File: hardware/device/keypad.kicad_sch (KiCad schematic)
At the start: 42 parts, among them SW1 TRIG1, SW10 TRIG10, SW11 TRIG11, SW12 TRIG12, SW13 TRIG13, SW14 TRIG14, SW15 TRIG15, SW16 TRIG16, SW17 WHEEL_BTN, SW18 HELP, SW19 LEFT_BTN, SW2 TRIG2, SW20 RIGHT_BTN, SW3 TRIG3, SW4 TRIG4, SW5 TRIG5, SW6 TRIG6, SW7 TRIG7, SW8 TRIG8, SW9 TRIG9, U25 TCA8418RTWR

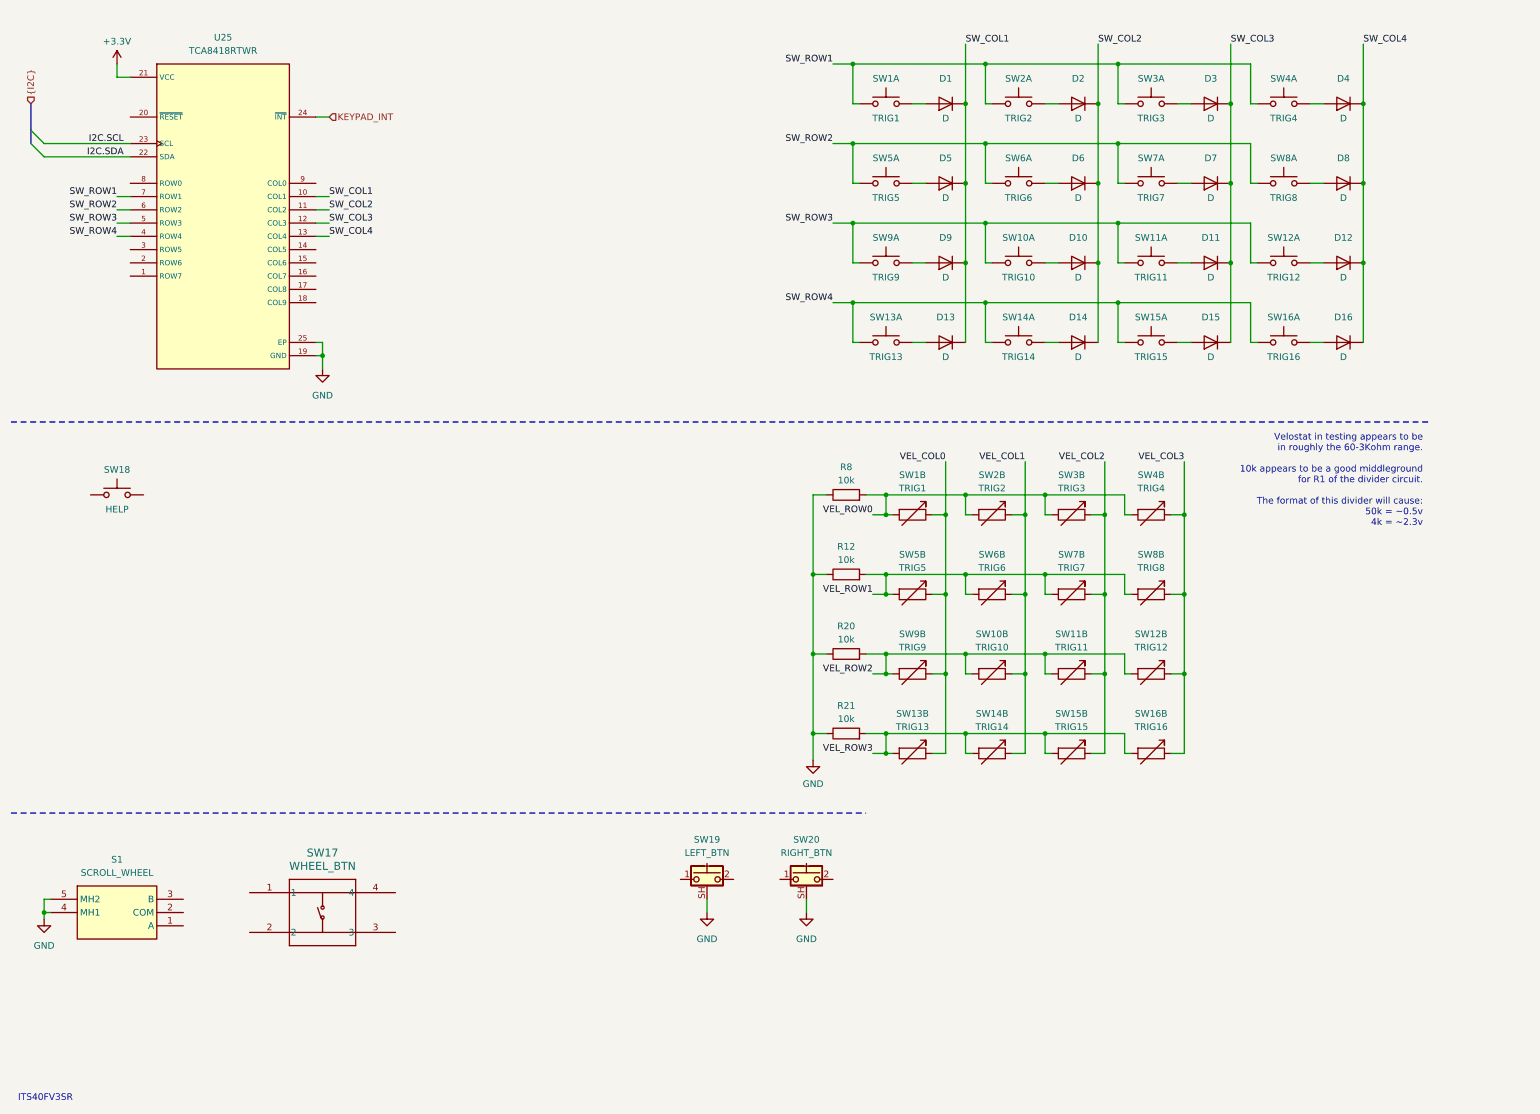
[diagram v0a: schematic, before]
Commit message: feat: resistor divider matrix for resistive touch
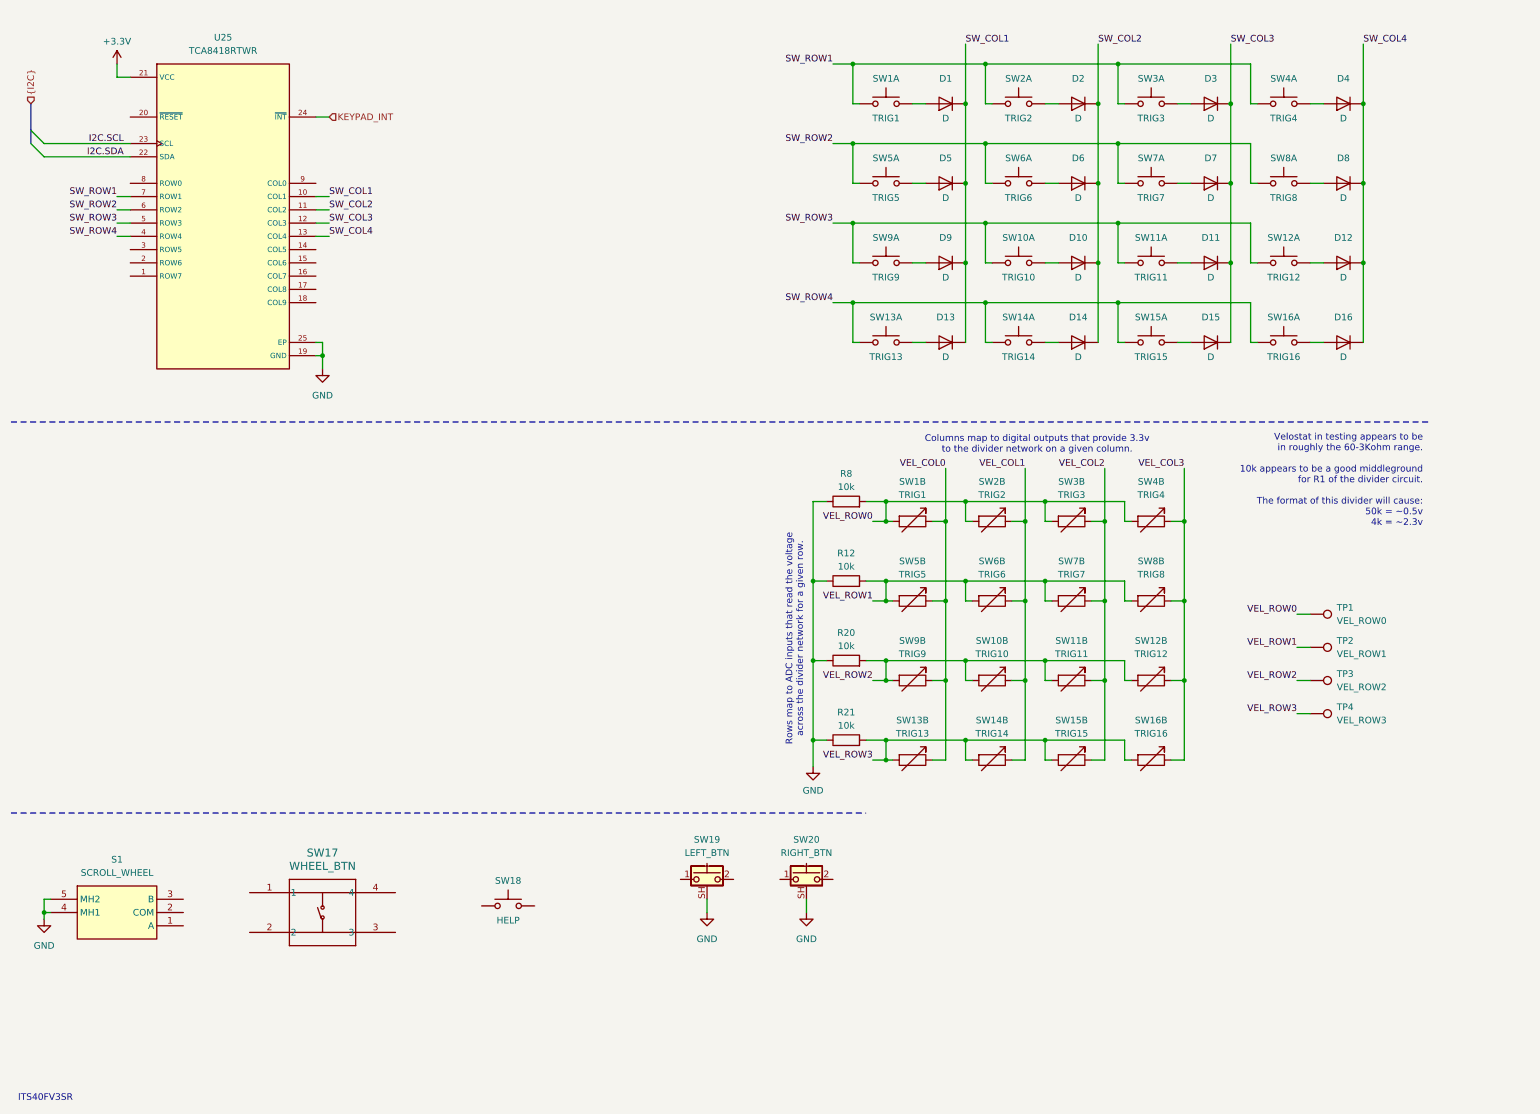
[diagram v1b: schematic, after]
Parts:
- added TP1: VEL_ROW0, symbol Connector:TestPoint
- added TP2: VEL_ROW1, symbol Connector:TestPoint
- added TP3: VEL_ROW2, symbol Connector:TestPoint
- added TP4: VEL_ROW3, symbol Connector:TestPoint
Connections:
- net VEL_ROW0: now also TP1.1
- net VEL_ROW1: now also TP2.1
- net VEL_ROW2: now also TP3.1
- net VEL_ROW3: now also TP4.1
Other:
- note added: "Columns map to digital outputs that provide 3.3v to the divider network on a given column."
- note added: "Rows map to ADC inputs that read the voltage across the divider network for a given row."
- moved on the sheet: R12, R20, R21, R8, SW10B, SW11B, SW12B, SW13B, SW14B, SW15B, SW16B, SW18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

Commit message: feat: keypad schematic organization
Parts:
- added TP5: VEL_COL0, TestPoint:TestPoint_Pad_D2.5mm, symbol Connector:TestPoint
- added TP6: VEL_COL1, TestPoint:TestPoint_Pad_D2.5mm, symbol Connector:TestPoint
- added TP7: VEL_COL2, TestPoint:TestPoint_Pad_D2.5mm, symbol Connector:TestPoint
- added TP8: VEL_COL3, TestPoint:TestPoint_Pad_D2.5mm, symbol Connector:TestPoint
- R12, R20, R21, R8: footprint (none) -> Resistor_SMD:R_0805_2012Metric
- TP1, TP2, TP3, TP4: footprint (none) -> TestPoint:TestPoint_Pad_D2.5mm
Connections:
- net SW_COL1: now also D10.1 (K), D14.1 (K), D2.1 (K), D6.1 (K); no longer D1.1 (K), D13.1 (K), D5.1 (K), D9.1 (K)
- net SW_COL2: now also D11.1 (K), D15.1 (K), D3.1 (K), D7.1 (K); no longer D10.1 (K), D14.1 (K), D2.1 (K), D6.1 (K)
- net SW_COL3: now also D12.1 (K), D16.1 (K), D4.1 (K), D8.1 (K); no longer D11.1 (K), D15.1 (K), D3.1 (K), D7.1 (K)
- net SW_ROW1: now also SW5.1, SW6.1, SW7.1, SW8.1; no longer SW1.1, SW2.1, SW3.1, SW4.1
- net SW_ROW2: now also SW10.1, SW11.1, SW12.1, SW9.1; no longer SW5.1, SW6.1, SW7.1, SW8.1
- net SW_ROW3: now also SW13.1, SW14.1, SW15.1, SW16.1; no longer SW10.1, SW11.1, SW12.1, SW9.1
- net VEL_COL0: now also TP5.1
- net VEL_COL1: now also TP6.1
- net VEL_COL2: now also TP7.1
- net VEL_COL3: now also TP8.1
- net SW_ROW0: now reaches U25.8 (ROW0)
- net SW_ROW0: now also SW1.1, SW2.1, SW3.1, SW4.1
- net SW_COL0: now reaches U25.9 (COL0)
- net SW_COL0: now also D1.1 (K), D13.1 (K), D5.1 (K), D9.1 (K)
- removed net SW_COL4: D12.1 (K), D16.1 (K), D4.1 (K), D8.1 (K), U25.13 (COL4)
- removed net SW_ROW4: SW13.1, SW14.1, SW15.1, SW16.1, U25.4 (ROW4)
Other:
- note added: "Columns map to digital outputs that provide 3.3v to the divider network on a given column. Unaddressed columns should be pulled to ground."
- note added: "Diodes prevent ghosting from 3 keys on adjacent rows and columns being simultaniously pressed."
- note added: "NOTE: Check circuit for crosstalk issues: https://www.mdpi.com/1424-8220/16/2/155"
- note added: "NOTE: Used larger package for fixed dividers to allow hand-soldering to change sensitivity during prototyping."
- note added: "TODO: add navigation stick? https://tech.alpsalpine.com/e/products/detail/RKJXT1F42001/#ancFig4"
- note added: "Velostat in testing appears to be in roughly the 60-3Kohm range, 10 to 20 kohm for R2 should be good. R2 of the divider is the resistors tied to ground on one side."
- note removed: "Columns map to digital outputs that provide 3.3v to the divider network on a given column."
- note removed: "Velostat in testing appears to be in roughly the 60-3Kohm range. 10k appears to be a good middleground for R1 of the divider circuit. The format of this divider will cause: 50k = ~0.5v 4k = ~2.3v"
- moved on the sheet: D1, D10, D11, D12, D13, D14, D15, D16, D2, D3, D4, D5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
